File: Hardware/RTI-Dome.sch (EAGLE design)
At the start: 38 parts, among them IC1 24AA128ST, IC2 74LVC244

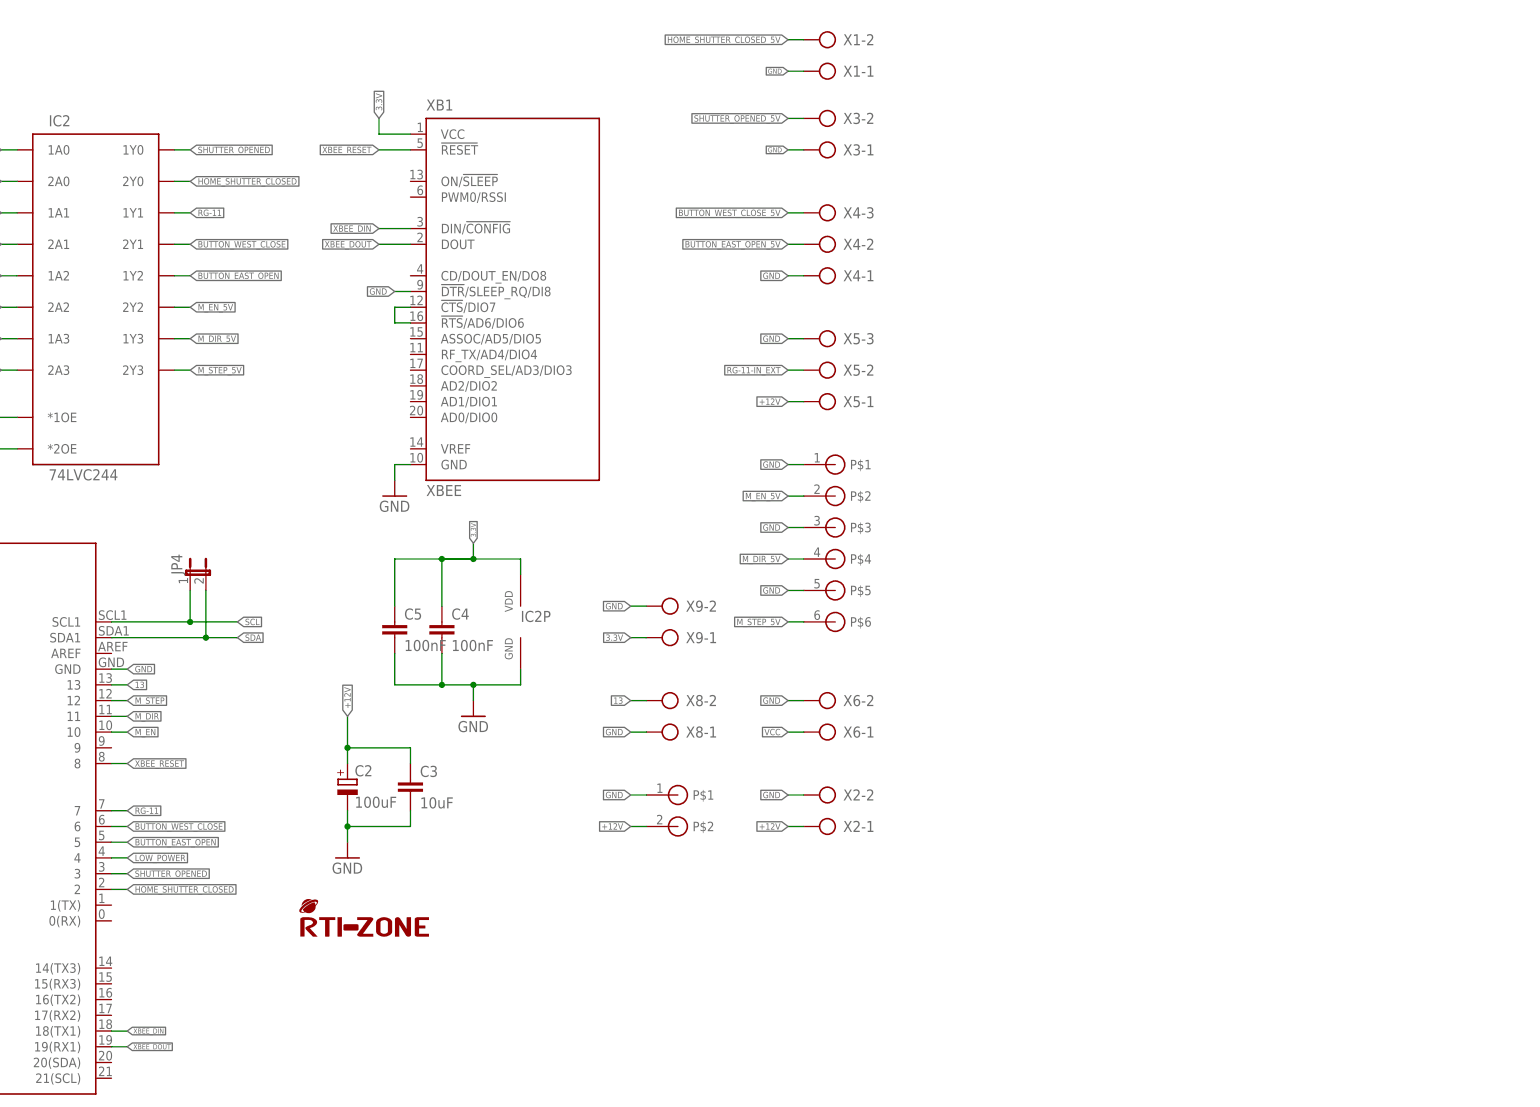
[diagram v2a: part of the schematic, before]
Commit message: Adding a usb-serial + usb port on SERIAL2 (pin 16 and 17)
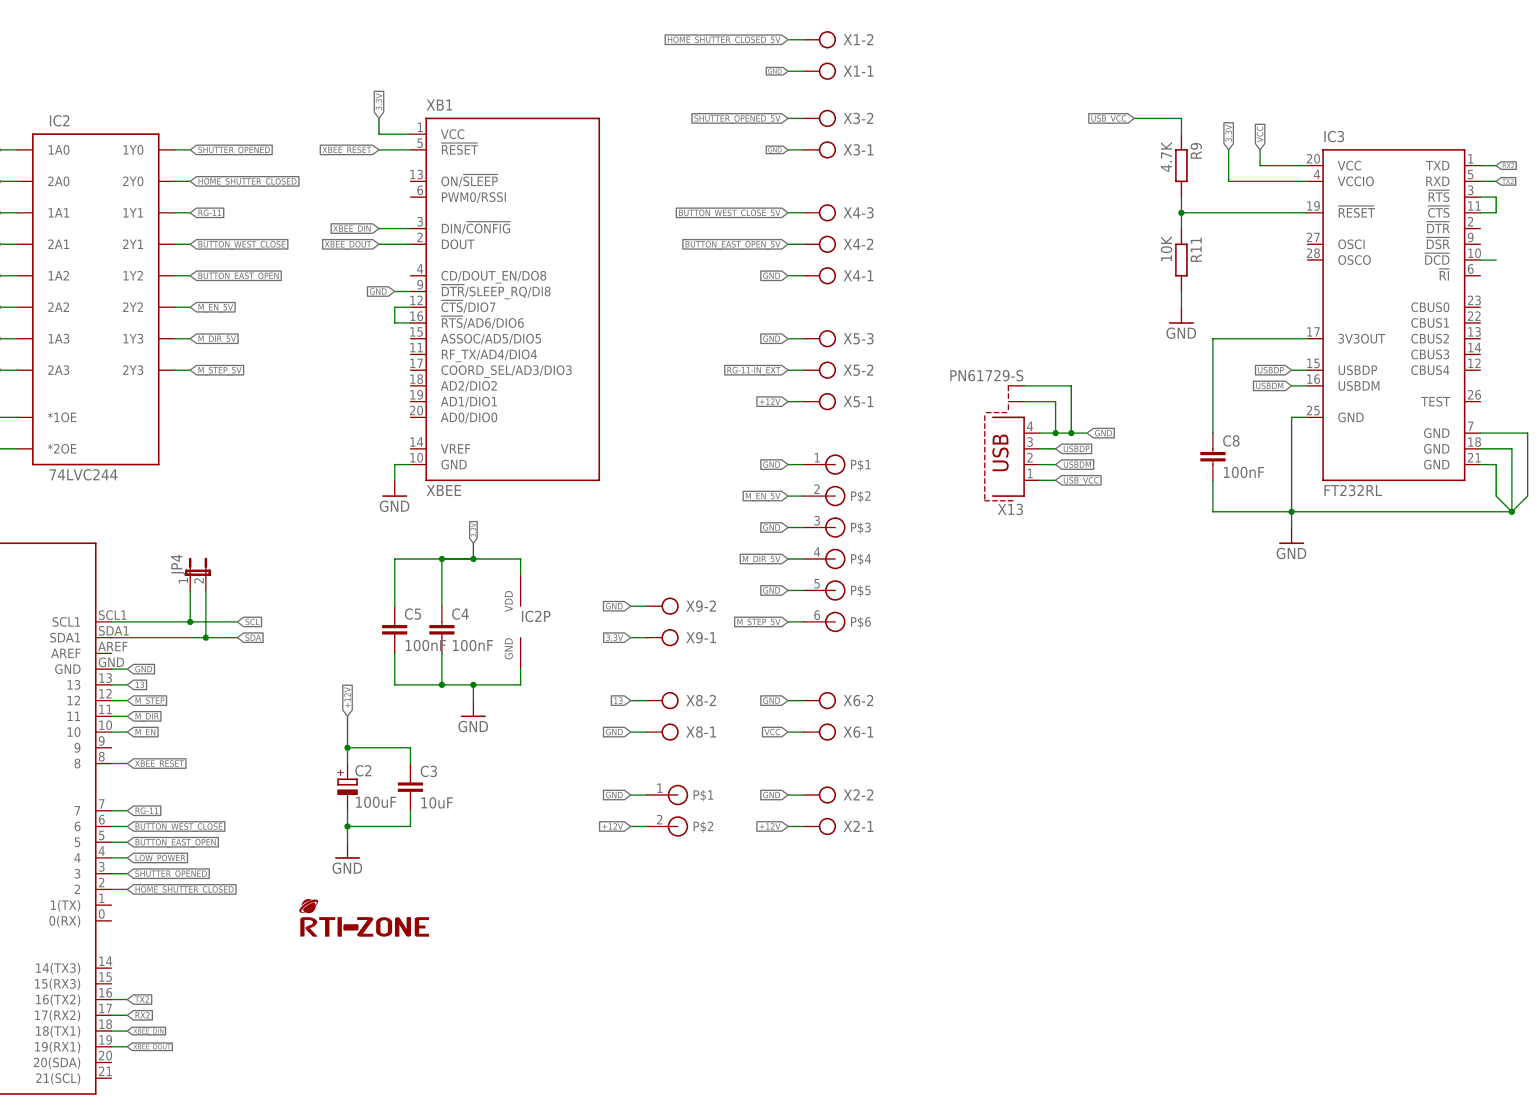
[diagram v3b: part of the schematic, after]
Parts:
- added C8: 100nF, rti:C-EU'0805'
- added IC3: FT232RL, ftdichip:FT232RL
- added R11: 10K, rti:R-EU'0805'
- added R9: 4.7K, rti:R-EU'0805'
- added X13: PN61729-S, con-berg:PN61729-S
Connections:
- new net N$1: IC3.!RESET, R11.1, R9.2
- new net N$21: IC3.!DCD
- new net N$4: IC3.!CTS, IC3.!RTS
- new net N$6: C8.1, IC3.3V3OUT
- new net RX2: IC3.TXD, PCB1.17(RX2)
- new net TX2: IC3.RXD, PCB1.16(TX2)
- new net USBDM: IC3.USBDM, X13.2
- new net USBDP: IC3.USBDP, X13.3
- new net USB_VCC: R9.1, X13.1
- net 3.3V: now also IC3.VCCIO
- net GND: now also C8.2, IC3.GND, IC3.GND@1, IC3.GND@2, IC3.GND@A, R11.2, X13.4, X13.S1, X13.S2
- net VCC: now also IC3.VCC
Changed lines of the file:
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@@
 <part name="C5" library="rti" deviceset="C-EU" device="'0805'" value="100nF"/>
 <part name="X9" library="con-ptr500" deviceset="AK500/2" device=""/>
+<part name="IC3" library="ftdichip" deviceset="FT232R" device="L"/>
+<part name="GND10" library="supply1" deviceset="GND" device=""/>
+<part name="R9" library="rti" deviceset="R-EU" device="'0805'" value="4.7K"/>
+<part name="R11" library="rti" deviceset="R-EU" device="'0805'" value="10K"/>
+<part name="GND11" library="supply1" deviceset="GND" device=""/>
+<part name="X13" library="con-berg" deviceset="PN61729-S" device=""/>
+<part name="C8" library="rti" deviceset="C-EU" device="'0805'" value="100nF"/>
 </parts>
 <sheets>
@@
 <instance part="X9" gate="-1" x="228.6" y="76.2" rot="R180"/>
 <instance part="X9" gate="-2" x="228.6" y="81.28" rot="R180"/>
+<instance part="IC3" gate="1" x="342.9" y="129.54"/>
+<instance part="GND10" gate="1" x="327.66" y="91.44"/>
+<instance part="R9" gate="G$1" x="309.88" y="152.4" rot="R270"/>
+<instance part="R11" gate="G$1" x="309.88" y="137.16" rot="R270"/>
+<instance part="GND11" gate="1" x="309.88" y="127"/>
+<instance part="X13" gate="G$1" x="284.48" y="106.68" rot="R180"/>
+<instance part="C8" gate="G$1" x="314.96" y="106.68"/>
 </instances>
 <busses>
@@
 <label x="220.98" y="81.28" size="1.016" layer="95" rot="R180" xref="yes"/>
 </segment>
+<segment>
+<pinref part="IC3" gate="1" pin="GND@1"/>
+<wire x1="358.14" y1="106.68" x2="363.22" y2="106.68" width="0.1524" layer="91"/>
+<wire x1="363.22" y1="106.68" x2="363.22" y2="96.52" width="0.1524" layer="91"/>
+<pinref part="IC3" gate="1" pin="GND"/>
+<wire x1="358.14" y1="109.22" x2="365.76" y2="109.22" width="0.1524" layer="91"/>
+<wire x1="365.76" y1="109.22" x2="365.76" y2="99.06" width="0.1524" layer="91"/>
+<wire x1="365.76" y1="99.06" x2="363.22" y2="96.52" width="0.1524" layer="91"/>
+<pinref part="IC3" gate="1" pin="GND@2"/>
+<wire x1="358.14" y1="104.14" x2="360.68" y2="104.14" width="0.1524" layer="91"/>
+<wire x1="360.68" y1="104.14" x2="360.68" y2="99.06" width="0.1524" layer="91"/>
+<wire x1="363.22" y1="96.52" x2="360.68" y2="99.06" width="0.1524" layer="91"/>
+<junction x="363.22" y="96.52"/>
+<pinref part="IC3" gate="1" pin="GND@A"/>
+<wire x1="330.2" y1="111.76" x2="327.66" y2="111.76" width="0.1524" layer="91"/>
+<wire x1="327.66" y1="111.76" x2="327.66" y2="96.52" width="0.1524" layer="91"/>
+<wire x1="327.66" y1="96.52" x2="327.66" y2="93.98" width="0.1524" layer="91"/>
+<wire x1="363.22" y1="96.52" x2="327.66" y2="96.52" width="0.1524" layer="91"/>
+<junction x="327.66" y="96.52"/>
+<pinref part="GND10" gate="1" pin="GND"/>
+<pinref part="C8" gate="G$1" pin="2"/>
+<wire x1="327.66" y1="96.52" x2="314.96" y2="96.52" width="0.1524" layer="91"/>
+<wire x1="314.96" y1="96.52" x2="314.96" y2="101.6" width="0.1524" layer="91"/>
+</segment>
+<segment>
+<pinref part="R11" gate="G$1" pin="2"/>
+<wire x1="309.88" y1="132.08" x2="309.88" y2="129.54" width="0.1524" layer="91"/>
+<pinref part="GND11" gate="1" pin="GND"/>
+</segment>
+<segment>
+<pinref part="X13" gate="G$1" pin="4"/>
+<wire x1="294.64" y1="109.22" x2="292.1" y2="109.22" width="0.1524" layer="91"/>
+<label x="294.64" y="109.22" size="1.016" layer="95" xref="yes"/>
+<pinref part="X13" gate="G$1" pin="S1"/>
+<wire x1="292.1" y1="109.22" x2="289.56" y2="109.22" width="0.1524" layer="91"/>
+<wire x1="289.56" y1="109.22" x2="287.02" y2="109.22" width="0.1524" layer="91"/>
+<wire x1="284.48" y1="114.3" x2="289.56" y2="114.3" width="0.1524" layer="91"/>
+<wire x1="289.56" y1="114.3" x2="289.56" y2="109.22" width="0.1524" layer="91"/>
+<junction x="289.56" y="109.22"/>
+<pinref part="X13" gate="G$1" pin="S2"/>
+<wire x1="284.48" y1="116.84" x2="292.1" y2="116.84" width="0.1524" layer="91"/>
+<wire x1="292.1" y1="116.84" x2="292.1" y2="109.22" width="0.1524" layer="91"/>
+<junction x="292.1" y="109.22"/>
+</segment>
 </net>
 <net name="+12V" class="1">
@@
 <wire x1="220.98" y1="76.2" x2="223.52" y2="76.2" width="0.1524" layer="91"/>
 <label x="220.98" y="76.2" size="1.016" layer="95" rot="R180" xref="yes"/>
+</segment>
+<segment>
+<pinref part="IC3" gate="1" pin="VCCIO"/>
+<wire x1="330.2" y1="149.86" x2="317.5" y2="149.86" width="0.1524" layer="91"/>
+<wire x1="317.5" y1="149.86" x2="317.5" y2="154.94" width="0.1524" layer="91"/>
+<label x="317.5" y="154.94" size="1.016" layer="95" rot="R90" xref="yes"/>
 </segment>
 </net>
@@
 <pinref part="X6" gate="-1" pin="KL"/>
 </segment>
+<segment>
+<pinref part="IC3" gate="1" pin="VCC"/>
+<wire x1="330.2" y1="152.4" x2="322.58" y2="152.4" width="0.1524" layer="91"/>
+<wire x1="322.58" y1="152.4" x2="322.58" y2="154.94" width="0.1524" layer="91"/>
+<label x="322.58" y="154.94" size="1.016" layer="95" rot="R90" xref="yes"/>
+</segment>
 </net>
 <net name="N$2" class="0">
@@
 </segment>
 </net>
+<net name="N$1" class="0">
+<segment>
+<pinref part="R9" gate="G$1" pin="2"/>
+<pinref part="R11" gate="G$1" pin="1"/>
+<wire x1="309.88" y1="147.32" x2="309.88" y2="144.78" width="0.1524" layer="91"/>
+<pinref part="IC3" gate="1" pin="!RESET"/>
+<wire x1="309.88" y1="144.78" x2="309.88" y2="142.24" width="0.1524" layer="91"/>
+<wire x1="330.2" y1="144.78" x2="309.88" y2="144.78" width="0.1524" layer="91"/>
+<junction x="309.88" y="144.78"/>
+</segment>
+</net>
+<net name="USB_VCC" class="0">
+<segment>
+<pinref part="X13" gate="G$1" pin="1"/>
+<wire x1="289.56" y1="101.6" x2="287.02" y2="101.6" width="0.1524" layer="91"/>
+<label x="289.56" y="101.6" size="1.016" layer="95" xref="yes"/>
+</segment>
+<segment>
+<pinref part="R9" gate="G$1" pin="1"/>
+<wire x1="302.26" y1="160.02" x2="309.88" y2="160.02" width="0.1524" layer="91"/>
+<wire x1="309.88" y1="160.02" x2="309.88" y2="157.48" width="0.1524" layer="91"/>
+<label x="302.26" y="160.02" size="1.016" layer="95" rot="R180" xref="yes"/>
+</segment>
+</net>
+<net name="USBDP" class="0">
+<segment>
+<pinref part="IC3" gate="1" pin="USBDP"/>
+<wire x1="327.66" y1="119.38" x2="330.2" y2="119.38" width="0.1524" layer="91"/>
+<label x="327.66" y="119.38" size="1.016" layer="95" rot="R180" xref="yes"/>
+</segment>
+<segment>
+<pinref part="X13" gate="G$1" pin="3"/>
+<wire x1="289.56" y1="106.68" x2="287.02" y2="106.68" width="0.1524" layer="91"/>
+<label x="289.56" y="106.68" size="1.016" layer="95" xref="yes"/>
+</segment>
+</net>
+<net name="USBDM" class="0">
+<segment>
+<pinref part="IC3" gate="1" pin="USBDM"/>
+<wire x1="327.66" y1="116.84" x2="330.2" y2="116.84" width="0.1524" layer="91"/>
+<label x="327.66" y="116.84" size="1.016" layer="95" rot="R180" xref="yes"/>
+</segment>
+<segment>
+<pinref part="X13" gate="G$1" pin="2"/>
+<wire x1="289.56" y1="104.14" x2="287.02" y2="104.14" width="0.1524" layer="91"/>
+<label x="289.56" y="104.14" size="1.016" layer="95" xref="yes"/>
+</segment>
+</net>
+<net name="N$6" class="0">
+<segment>
+<pinref part="IC3" gate="1" pin="3V3OUT"/>
+<wire x1="330.2" y1="124.46" x2="314.96" y2="124.46" width="0.1524" layer="91"/>
+<wire x1="314.96" y1="124.46" x2="314.96" y2="109.22" width="0.1524" layer="91"/>
+<pinref part="C8" gate="G$1" pin="1"/>
+</segment>
+</net>
+<net name="N$21" class="0">
+<segment>
+<pinref part="IC3" gate="1" pin="!DCD"/>
+<wire x1="360.68" y1="137.16" x2="358.14" y2="137.16" width="0.1524" layer="91"/>
+</segment>
+</net>
+<net name="N$4" class="0">
+<segment>
+<pinref part="IC3" gate="1" pin="!RTS"/>
+<wire x1="358.14" y1="147.32" x2="360.68" y2="147.32" width="0.1524" layer="91"/>
+<wire x1="360.68" y1="147.32" x2="360.68" y2="144.78" width="0.1524" layer="91"/>
+<pinref part="IC3" gate="1" pin="!CTS"/>
+<wire x1="360.68" y1="144.78" x2="358.14" y2="144.78" width="0.1524" layer="91"/>
+</segment>
+</net>
+<net name="RX2" class="0">
+<segment>
+<pinref part="IC3" gate="1" pin="TXD"/>
+<wire x1="360.68" y1="152.4" x2="358.14" y2="152.4" width="0.1524" layer="91"/>
+<label x="360.68" y="152.4" size="0.8128" layer="95" xref="yes"/>
+</segment>
+<segment>
+<pinref part="PCB1" gate="G$1" pin="17(RX2)"/>
+<wire x1="139.7" y1="15.24" x2="137.16" y2="15.24" width="0.1524" layer="91"/>
+<label x="139.7" y="15.24" size="1.016" layer="95" xref="yes"/>
+</segment>
+</net>
+<net name="TX2" class="0">
+<segment>
+<pinref part="IC3" gate="1" pin="RXD"/>
+<wire x1="360.68" y1="149.86" x2="358.14" y2="149.86" width="0.1524" layer="91"/>
+<label x="360.68" y="149.86" size="0.8128" layer="95" xref="yes"/>
+</segment>
+<segment>
+<pinref part="PCB1" gate="G$1" pin="16(TX2)"/>
+<wire x1="139.7" y1="17.78" x2="137.16" y2="17.78" width="0.1524" layer="91"/>
+<label x="139.7" y="17.78" size="1.016" layer="95" xref="yes"/>
+</segment>
+</net>

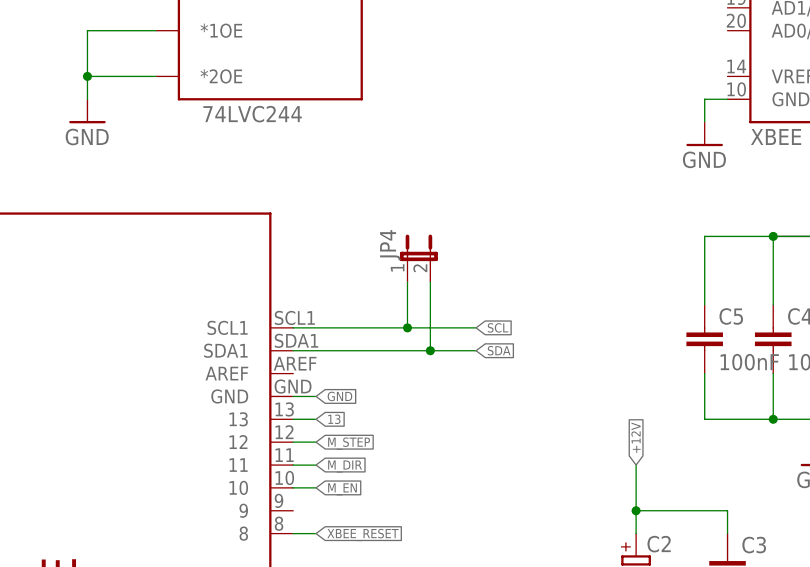
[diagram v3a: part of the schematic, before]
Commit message: Remove I2C 2 pin header as we now have the eeprom on the board.
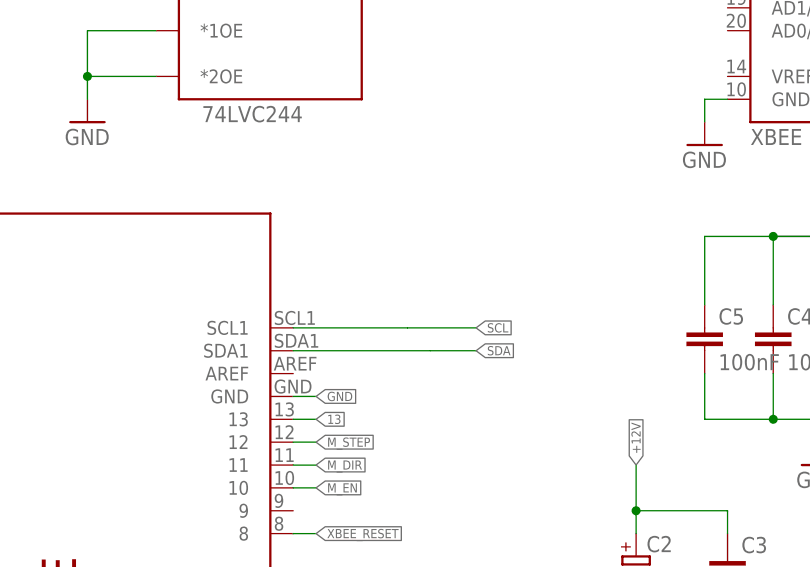
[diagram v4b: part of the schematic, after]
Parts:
- removed JP4: (no value), jumper:JP1E
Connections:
- net SCL: no longer JP4.1
- net SDA: no longer JP4.2
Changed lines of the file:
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@@
 <part name="R5" library="rti" deviceset="R-EU" device="'0805'" value="100"/>
 <part name="FRAME1" library="frames" deviceset="DINA4_L" device=""/>
-<part name="JP4" library="jumper" deviceset="JP1E" device=""/>
 <part name="U$4" library="rti" deviceset="RTI-LOGO" device="_BIG" value="RTI-LOGO_BIG"/>
 <part name="C2" library="rti" deviceset="CPOL-EU" device="" value="100uF"/>
@@
 <instance part="FRAME1" gate="G$1" x="0" y="0"/>
 <instance part="FRAME1" gate="G$2" x="162.56" y="0"/>
-<instance part="JP4" gate="A" x="149.86" y="86.36"/>
 <instance part="U$4" gate="G$1" x="167.64" y="27.94"/>
 <instance part="C2" gate="G$1" x="175.26" y="53.34"/>
@@
 <net name="SDA" class="0">
 <segment>
-<pinref part="JP4" gate="A" pin="2"/>
 <wire x1="137.16" y1="76.2" x2="152.4" y2="76.2" width="0.1524" layer="91"/>
-<wire x1="152.4" y1="76.2" x2="152.4" y2="83.82" width="0.1524" layer="91"/>
 <pinref part="PCB1" gate="G$1" pin="SDA1"/>
 <wire x1="152.4" y1="76.2" x2="157.48" y2="76.2" width="0.1524" layer="91"/>
-<junction x="152.4" y="76.2"/>
 <label x="157.48" y="76.2" size="1.016" layer="95" xref="yes"/>
 </segment>
@@
 </segment>
 <segment>
-<pinref part="JP4" gate="A" pin="1"/>
 <wire x1="137.16" y1="78.74" x2="149.86" y2="78.74" width="0.1524" layer="91"/>
-<wire x1="149.86" y1="78.74" x2="149.86" y2="83.82" width="0.1524" layer="91"/>
 <pinref part="PCB1" gate="G$1" pin="SCL1"/>
 <wire x1="149.86" y1="78.74" x2="157.48" y2="78.74" width="0.1524" layer="91"/>
-<junction x="149.86" y="78.74"/>
 <label x="157.48" y="78.74" size="1.016" layer="95" xref="yes"/>
 </segment>

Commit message: Only focus on doing one board with terminal header. Removed the old one with STL connectors.
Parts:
- removed U$2: STL-140-2, rti:STL-140-2
- removed U$3: STL-140-6, rti:STL-140-6
- added C6, C7, C9: 100nF, rti:C-EU'0805'
- added IC4: 74ABT244, rti:74LVC244
- added R12, R20: 1K, rti:R-EU'0805'
- added R21: 4.7K, rti:R-EU'0805'
- added X10: (no value), con-ptr500:AK500/3
- added X11, X12: (no value), con-ptr500:AK500/2
- X9: device con-ptr500:AK500/2 -> con-ptr500:AK500/3
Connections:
- removed net 13: PCB1.13, X8-2.KL
- new net AT_PARK_PIN_EXT: IC2G$1.1A3, R20.1, X7-2.KL
- new net AT_PARK_PIN_LOOP_EXT: IC4G$1.2Y1, R12.1, X7-3.KL
- new net D13: IC2G$1.2Y3, PCB1.13
- new net D13_EXT: IC2G$1.2A3, R21.2, X8-2.KL
- net +12V: now also X11-2.KL; no longer U$2.P$2
- net 3.3V: now also C9.1, X12-2.KL; no longer X9-1.KL
- net AT_PARK_PIN: now also IC2G$1.1Y3; no longer X7-2.KL
- net AT_PARK_PIN_LOOP: now also IC4G$1.2A1; no longer X7-3.KL
- net GND: now also C6.2, C7.2, C9.2, IC4G$1.*1OE, IC4G$1.*2OE, IC4P.GND, X10-2.KL, X11-1.KL, X12-1.KL, X6-1.KL, X9-1.KL, X9-3.KL; no longer U$2.P$1, U$3.P$1, U$3.P$3, U$3.P$5, X6-2.KL, X9-2.KL
- net M_DIR: now also IC4G$1.2A0; no longer IC2G$1.1A3
- net M_DIR_5V: now also IC4G$1.2Y0, X10-1.KL; no longer IC2G$1.1Y3, U$3.P$4
- net M_EN: now also IC4G$1.1A0; no longer IC2G$1.2A2
- net M_EN_5V: now also IC4G$1.1Y0, X9-2.KL; no longer IC2G$1.2Y2, U$3.P$2
- net M_STEP: now also IC4G$1.1A1; no longer IC2G$1.2A3
- net M_STEP_5V: now also IC4G$1.1Y1, X10-3.KL; no longer IC2G$1.2Y3, U$3.P$6
- net VCC: now also C6.1, C7.1, IC4P.VDD, R12.2, R20.2, R21.1, X6-2.KL; no longer X6-1.KL
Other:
- moved on the sheet: C1, C2, C3, C4, C5, C8, IC1, IC2, IC2P, IC3, R1, R10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

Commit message: All pull-up for external pinsare now 4.7K
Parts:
- R12, R13, R14, R19, R20: value 1K -> 4.7K
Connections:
- net GND: now also IC2G$1.2A2, IC4G$1.1A2, IC4G$1.1A3, IC4G$1.2A2, IC4G$1.2A3
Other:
- note added: "3.3V -> 5V"
- note added: "5V->3.3V"
- moved on the sheet: C1, C2, C3, C4, C5, C6, C7, C8, C9, IC1, IC2, IC2P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
